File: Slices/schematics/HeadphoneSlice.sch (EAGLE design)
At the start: 50 parts, among them IC1 QUAD_OPAMPD, IC3 RC4560, Q1 SI2309CDS, Q2 BSS123, X1 1503_09

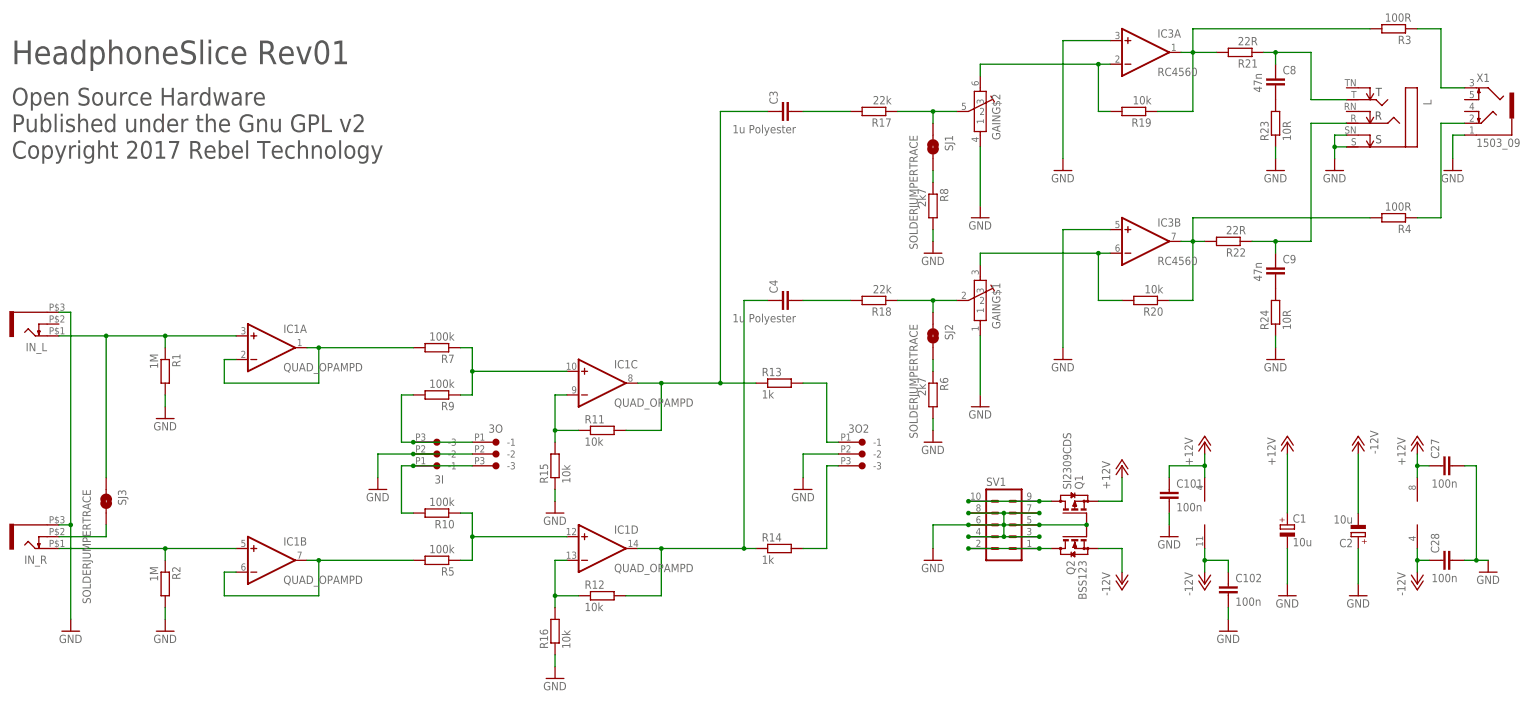
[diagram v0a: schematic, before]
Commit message: changed to inv summing op amp and change through bus to second input
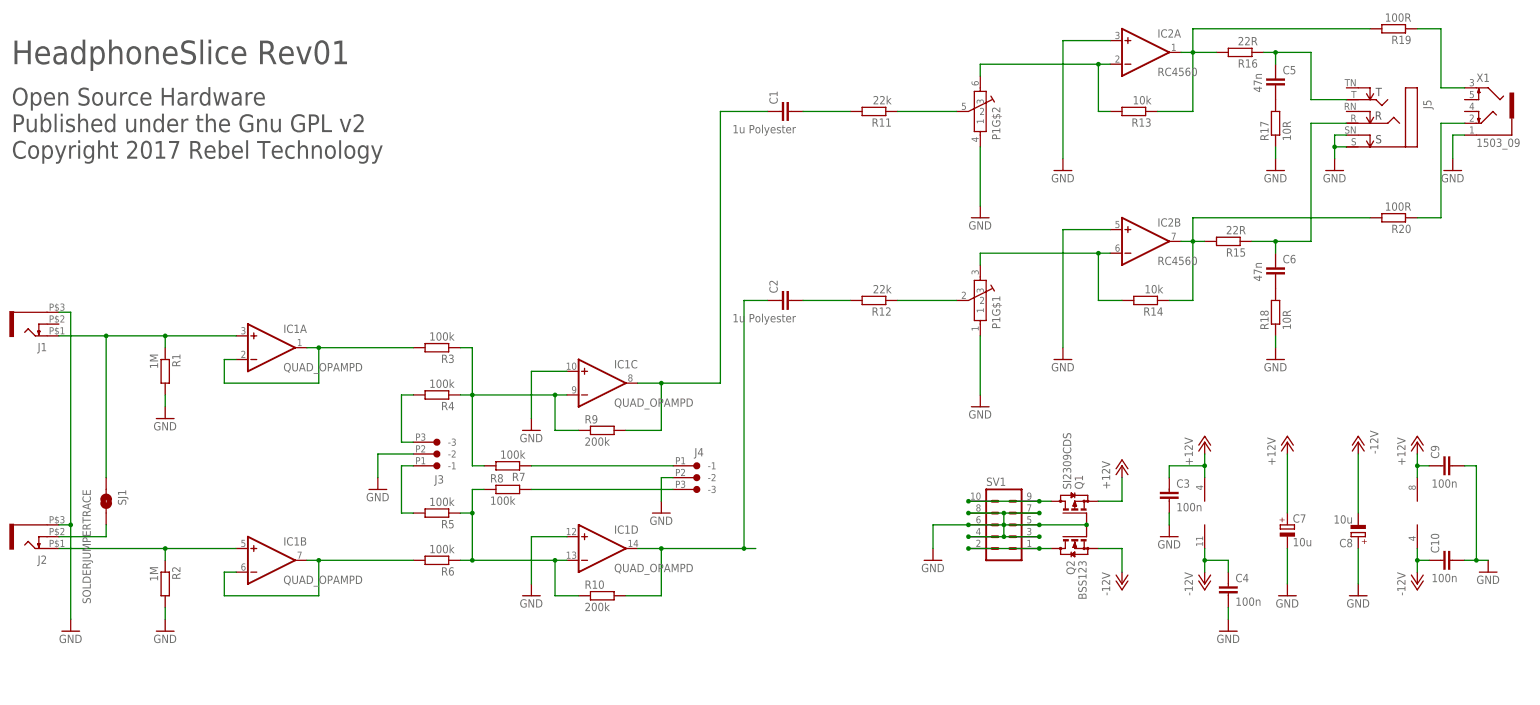
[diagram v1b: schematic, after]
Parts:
- removed 3O, 3O2: CON-JST_PH_3W, Rebel:CON-JST_PH_3W
- removed C101, C102, C27: 100n, Rebel:C-EUC0603
- removed L: NEUTRIK_NMJ6HCD2, neutrik_jacks:NEUTRIK_NMJ6HCD2
- removed R21, R22: 22R, Rebel:R-EU_0603
- removed R23, R24: 10R, Rebel:R-EU_0603
- removed SJ2, SJ3: SOLDERJUMPERTRACE, SparkFun:SOLDERJUMPERTRACE
- added C5, C6: 47n, Rebel:C-EUC0603
- added C7: 10u, rcl:CPOL-EU153CLV-0505
- added J4: CON-JST_PH_3W, Rebel:CON-JST_PH_3W
- added J5: NEUTRIK_NRJ6HFSTD, neutrik_jacks:NEUTRIK_NRJ6HFSTD
- C1, C2: value 10u -> 1u Polyester; device rcl:CPOL-EU153CLV-0505 -> Rebel:C-EUC1210
- C3, C4: value 1u Polyester -> 100n; device Rebel:C-EUC1210 -> Rebel:C-EUC0603
- C8: value 47n -> 10u; device Rebel:C-EUC0603 -> rcl:CPOL-EU153CLV-0505
- C9: value 47n -> 100n
- R10, R9: value 100k -> 200k
- R11, R12: value 10k -> 22k
- R13, R14: value 1k -> 10k
- R15, R16: value 10k -> 22R
- R17, R18: value 22k -> 10R
- R19, R20: value 10k -> 100R
- R3, R4: value 100R -> 100k
- R6, R8: value 2k7 -> 100k
- renumbered 3I to J3, C28 to C10, GAIN to P1, IC3 to IC2, IN_L to J1, IN_R to J2
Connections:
- removed net BUS_OUT_L: 3O2.-1, R13.2
- removed net BUS_OUT_R: 3O2.-3, R14.2
- removed net N$15: R6.1, SJ2.2
- removed net N$17: IC1C.-IN, R11.1, R15.2
- removed net N$18: IC1D.-IN, R12.1, R16.2
- removed net N$9: R8.1, SJ1.2
- new net N$20: J4.-1, R7.1
- new net N$22: J4.-3, R8.2
- net +12V: now also C3.1, C7.+, C9.1; no longer C1.+, C101.1, C27.1
- net -12V: now also C4.1, C8.-; no longer C102.1, C2.-
- net BUS_IN_L: now also R4.2; no longer 3O.-1, R9.2
- net BUS_IN_R: now also R5.2; no longer 3O.-3, R10.2
- net GND: now also C3.2, C4.2, C7.-, C8.+, C9.2, IC1C.+IN, IC1D.+IN, J4.-2, J5.S, J5.SN, R17.1, R18.1; no longer 3O.-2, 3O2.-2, C1.-, C101.2, C102.2, C2.+, C27.2, L.S, L.SN, R15.1, R16.1, R23.1, R24.1, R6.2, R8.2
- net HP_L: now also C5.1, J5.T, R16.1; no longer C8.1, L.T, R21.1
- net HP_R: now also C6.1, J5.R, R15.1; no longer C9.1, L.R, R22.1
- net IN_B1: now also SJ1.2; no longer SJ3.2
- net IN_L: now also SJ1.1; no longer SJ3.1
- net LINE_L: now also R19.1; no longer R3.1
- net LINE_R: now also R20.1; no longer R4.1
- net N$10: now also C1.1, R9.2; no longer C3.1, R11.2, R13.1
- net N$11: now also R6.2; no longer R5.2
- net N$12: now also C6.2, R18.2; no longer C9.2, R24.2
- net N$13: now also R3.2; no longer R7.2
- net N$16: now also R14.2; no longer R20.2
- net N$19: now also R13.1, R16.2, R19.2; no longer R19.1, R21.2, R3.2
- net N$2: now also R14.1, R15.2, R20.2; no longer R20.1, R22.2, R4.2
- net N$21: now also C5.2, R17.2; no longer C8.2, R23.2
- net N$3: now also R13.2; no longer R19.2
- net N$4: now also C2.2, R12.2; no longer C4.2, R18.2
- net N$45: now also IC1D.-IN, R6.1, R8.1; no longer IC1D.+IN
- net N$5: now also R11.1; no longer R17.1, SJ1.1
- net N$50: now also IC1C.-IN, R3.1, R4.1, R7.2; no longer IC1C.+IN, R7.1
- net N$6: now also R12.1; no longer R18.1, SJ2.1
- net N$7: now also C2.1, R10.2; no longer C4.1, R12.2, R14.1
- net N$8: now also C1.2, R11.2; no longer C3.2, R17.2
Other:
- moved on the sheet: C3, C4, C9, R10, R11, R12, R13, R14, R15, R16, R17, R18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

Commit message: reduced module depth
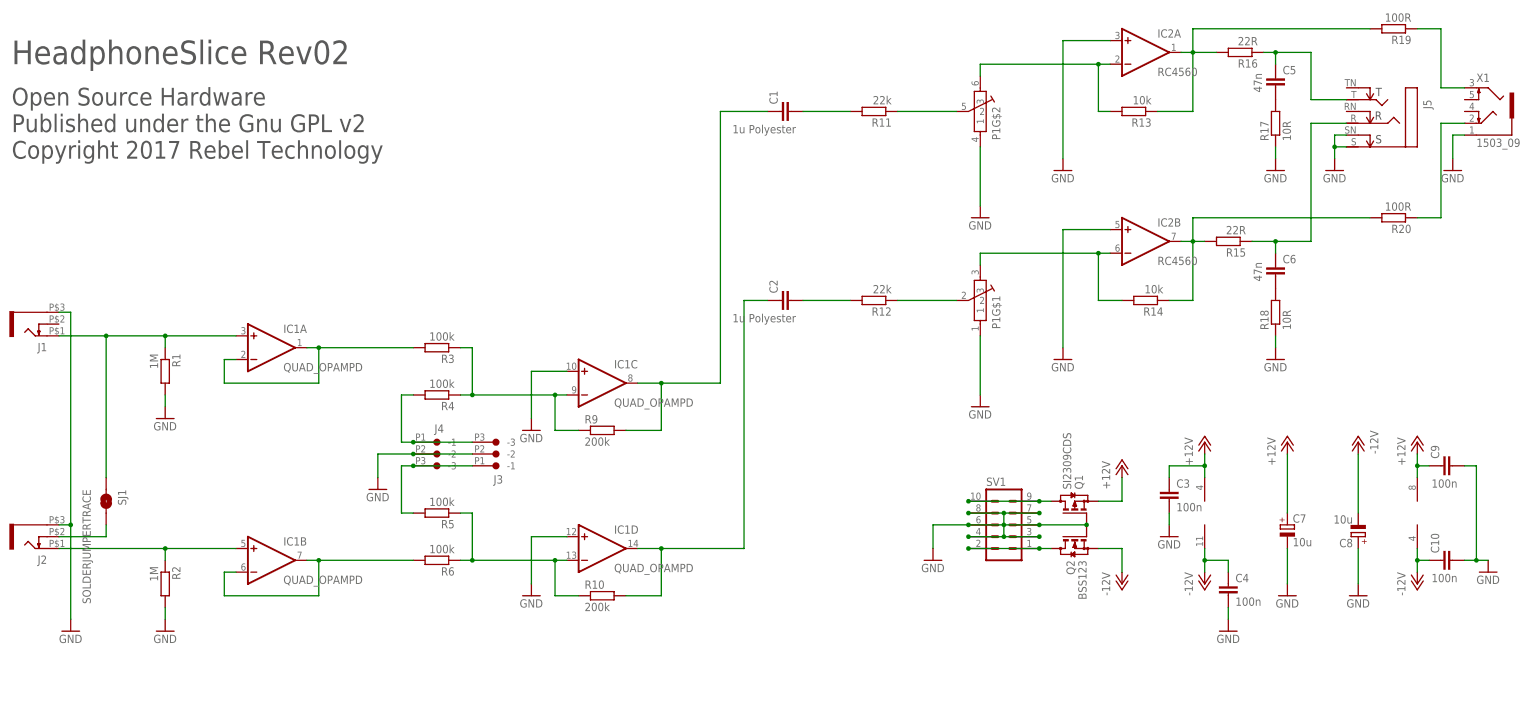
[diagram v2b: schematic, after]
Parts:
- removed R7, R8: 100k, Rebel:R-EU_0603
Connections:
- removed net N$20: J4.-1, R7.1
- removed net N$22: J4.-3, R8.2
- net BUS_IN_L: now also J4.-1
- net BUS_IN_R: now also J4.-3
- net N$45: no longer R8.1
- net N$50: no longer R7.2
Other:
- note added: "HeadphoneSlice Rev02"
- note removed: "HeadphoneSlice Rev01"
- moved on the sheet: J3, J4
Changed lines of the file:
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@@
 <part name="R19" library="Rebel" deviceset="R-EU_" device="0603" value="100R"/>
 <part name="R20" library="Rebel" deviceset="R-EU_" device="0603" value="100R"/>
-<part name="R7" library="Rebel" deviceset="R-EU_" device="0603" value="100k"/>
-<part name="R8" library="Rebel" deviceset="R-EU_" device="0603" value="100k"/>
-<part name="GND7" library="supply1" deviceset="GND" device=""/>
 <part name="GND5" library="supply1" deviceset="GND" device=""/>
 <part name="GND6" library="supply1" deviceset="GND" device=""/>
@@
 Published under the Gnu GPL v2
 Copyright 2017 Rebel Technology</text>
-<text x="-93.98" y="157.48" size="5.08" layer="97">HeadphoneSlice Rev01</text>
+<text x="-93.98" y="157.48" size="5.08" layer="97">HeadphoneSlice Rev02</text>
 </plain>
 <instances>
@@
 </instance>
 <instance part="GND21" gate="1" x="223.52" y="48.26"/>
-<instance part="J3" gate="G$1" x="-7.62" y="71.12" rot="R180"/>
+<instance part="J3" gate="G$1" x="5.08" y="71.12" rot="R180"/>
 <instance part="C1" gate="G$1" x="71.12" y="147.32" smashed="yes" rot="R90">
 <attribute name="NAME" x="70.739" y="148.844" size="1.778" layer="95" rot="R90"/>
@@
 <instance part="P1" gate="G$1" x="114.3" y="106.68" rot="MR90"/>
 <instance part="P1" gate="G$2" x="114.3" y="147.32" rot="MR90"/>
-<instance part="J4" gate="G$1" x="48.26" y="71.12" rot="MR0"/>
+<instance part="J4" gate="G$1" x="-7.62" y="76.2" rot="MR0"/>
 <instance part="R19" gate="G$1" x="203.2" y="165.1" rot="R180"/>
 <instance part="R20" gate="G$1" x="203.2" y="124.46" rot="R180"/>
-<instance part="R7" gate="G$1" x="12.7" y="71.12" rot="R180"/>
-<instance part="R8" gate="G$1" x="12.7" y="66.04"/>
-<instance part="GND7" gate="1" x="45.72" y="60.96"/>
 <instance part="GND5" gate="1" x="17.78" y="78.74"/>
 <instance part="GND6" gate="1" x="17.78" y="43.18"/>
@@
 <wire x1="-15.24" y1="73.66" x2="-15.24" y2="68.58" width="0.1524" layer="91"/>
 <pinref part="J3" gate="G$1" pin="-2"/>
+<pinref part="J4" gate="G$1" pin="-2"/>
+<junction x="-7.62" y="73.66"/>
+<wire x1="-7.62" y1="73.66" x2="5.08" y2="73.66" width="0.1524" layer="91"/>
 </segment>
 <segment>
@@
 </segment>
 <segment>
-<pinref part="J4" gate="G$1" pin="-2"/>
-<pinref part="GND7" gate="1" pin="GND"/>
-<wire x1="48.26" y1="68.58" x2="45.72" y2="68.58" width="0.1524" layer="91"/>
-<wire x1="45.72" y1="68.58" x2="45.72" y2="63.5" width="0.1524" layer="91"/>
-</segment>
-<segment>
 <pinref part="IC1" gate="C" pin="+IN"/>
 <pinref part="GND5" gate="1" pin="GND"/>
@@
 <wire x1="2.54" y1="50.8" x2="5.08" y2="50.8" width="0.1524" layer="91"/>
 <wire x1="5.08" y1="60.96" x2="5.08" y2="50.8" width="0.1524" layer="91"/>
-<pinref part="R8" gate="G$1" pin="1"/>
-<wire x1="7.62" y1="66.04" x2="5.08" y2="66.04" width="0.1524" layer="91"/>
-<wire x1="5.08" y1="66.04" x2="5.08" y2="60.96" width="0.1524" layer="91"/>
-<junction x="5.08" y="60.96"/>
 <pinref part="R10" gate="G$1" pin="1"/>
 <wire x1="22.86" y1="50.8" x2="22.86" y2="43.18" width="0.1524" layer="91"/>
@@
 <wire x1="2.54" y1="96.52" x2="5.08" y2="96.52" width="0.1524" layer="91"/>
 <wire x1="5.08" y1="96.52" x2="5.08" y2="86.36" width="0.1524" layer="91"/>
-<pinref part="R7" gate="G$1" pin="2"/>
-<wire x1="7.62" y1="71.12" x2="5.08" y2="71.12" width="0.1524" layer="91"/>
-<wire x1="5.08" y1="71.12" x2="5.08" y2="86.36" width="0.1524" layer="91"/>
 <junction x="5.08" y="86.36"/>
 <pinref part="R9" gate="G$1" pin="1"/>
@@
 <wire x1="38.1" y1="43.18" x2="45.72" y2="43.18" width="0.1524" layer="91"/>
 <wire x1="45.72" y1="43.18" x2="45.72" y2="53.34" width="0.1524" layer="91"/>
-<wire x1="66.04" y1="53.34" x2="63.5" y2="53.34" width="0.1524" layer="91"/>
 <pinref part="R10" gate="G$1" pin="2"/>
 <wire x1="63.5" y1="53.34" x2="45.72" y2="53.34" width="0.1524" layer="91"/>
@@
 <wire x1="68.58" y1="106.68" x2="63.5" y2="106.68" width="0.1524" layer="91"/>
 <wire x1="63.5" y1="106.68" x2="63.5" y2="53.34" width="0.1524" layer="91"/>
-<junction x="63.5" y="53.34"/>
 </segment>
 </net>
@@
 <wire x1="-10.16" y1="76.2" x2="-7.62" y2="76.2" width="0.1524" layer="91"/>
 <pinref part="J3" gate="G$1" pin="-3"/>
+<pinref part="J4" gate="G$1" pin="-1"/>
+<junction x="-7.62" y="76.2"/>
+<wire x1="-7.62" y1="76.2" x2="5.08" y2="76.2" width="0.1524" layer="91"/>
 </segment>
 </net>
@@
 <wire x1="-10.16" y1="71.12" x2="-10.16" y2="60.96" width="0.1524" layer="91"/>
 <pinref part="J3" gate="G$1" pin="-1"/>
-</segment>
-</net>
-<net name="N$20" class="0">
-<segment>
-<pinref part="J4" gate="G$1" pin="-1"/>
-<pinref part="R7" gate="G$1" pin="1"/>
-<wire x1="17.78" y1="71.12" x2="48.26" y2="71.12" width="0.1524" layer="91"/>
-</segment>
-</net>
-<net name="N$22" class="0">
-<segment>
 <pinref part="J4" gate="G$1" pin="-3"/>
-<pinref part="R8" gate="G$1" pin="2"/>
-<wire x1="17.78" y1="66.04" x2="48.26" y2="66.04" width="0.1524" layer="91"/>
-</segment>
-</net>
+<junction x="-7.62" y="71.12"/>
+<wire x1="-7.62" y1="71.12" x2="5.08" y2="71.12" width="0.1524" layer="91"/>
+</segment>
+</net>
